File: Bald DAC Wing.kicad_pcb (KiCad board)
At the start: 4 copper layers, 62.2 x 46.5 mm, 46 parts, among them J1 PWR, J10 Ctrl Debug, J11 BNC_B, J13 Feather Debug, J2 DAC_A_Out, J3 DAC_B_Out, J4 BNC_Z, J5 Z_Out, J6 Feather, J7 Data Debug Low, J8 BNC_A, J9 Data Debug High, U1 AD5447, U2 AD8065ARTZ, U3 AD8065ARTZ, U4 74LVC574APWR, U5 74LVC574APWR, U6 74LVC1G04, U7 REF3425

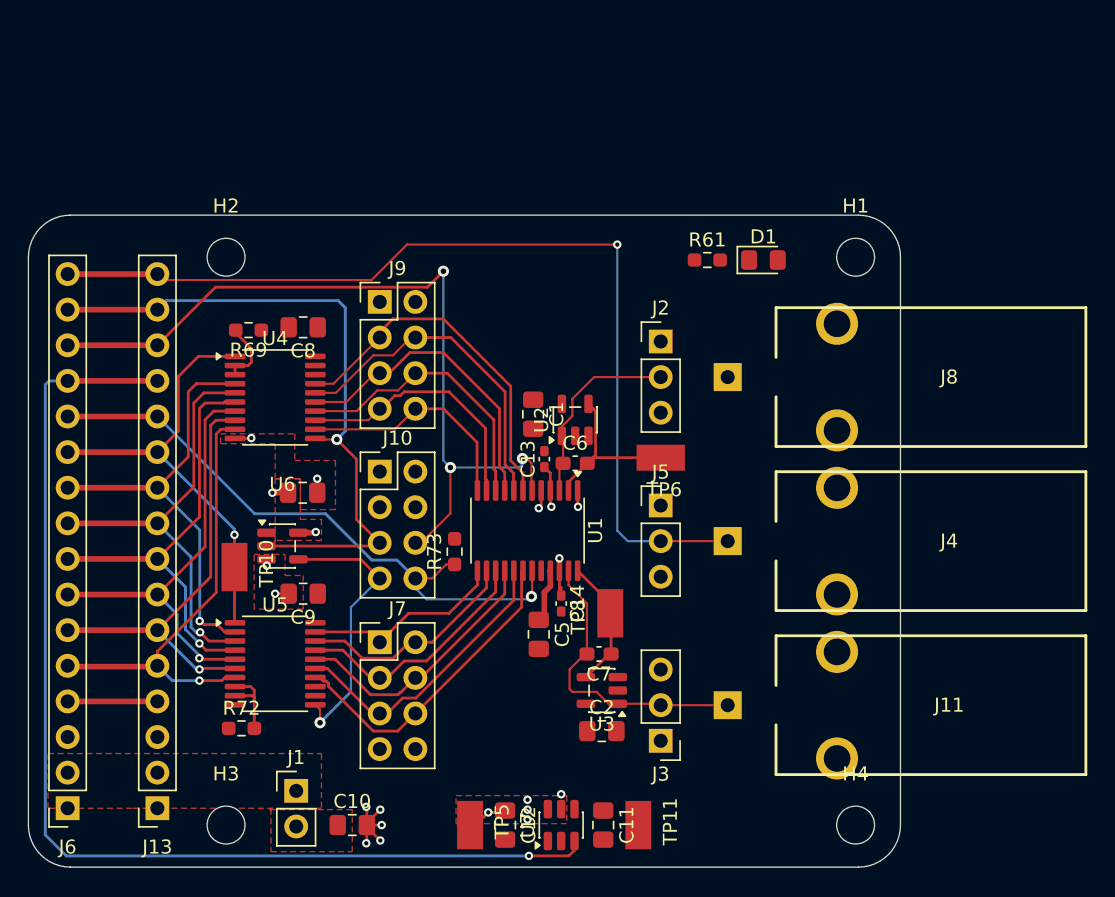
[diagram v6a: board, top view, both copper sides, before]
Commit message: time to clean-up silks.
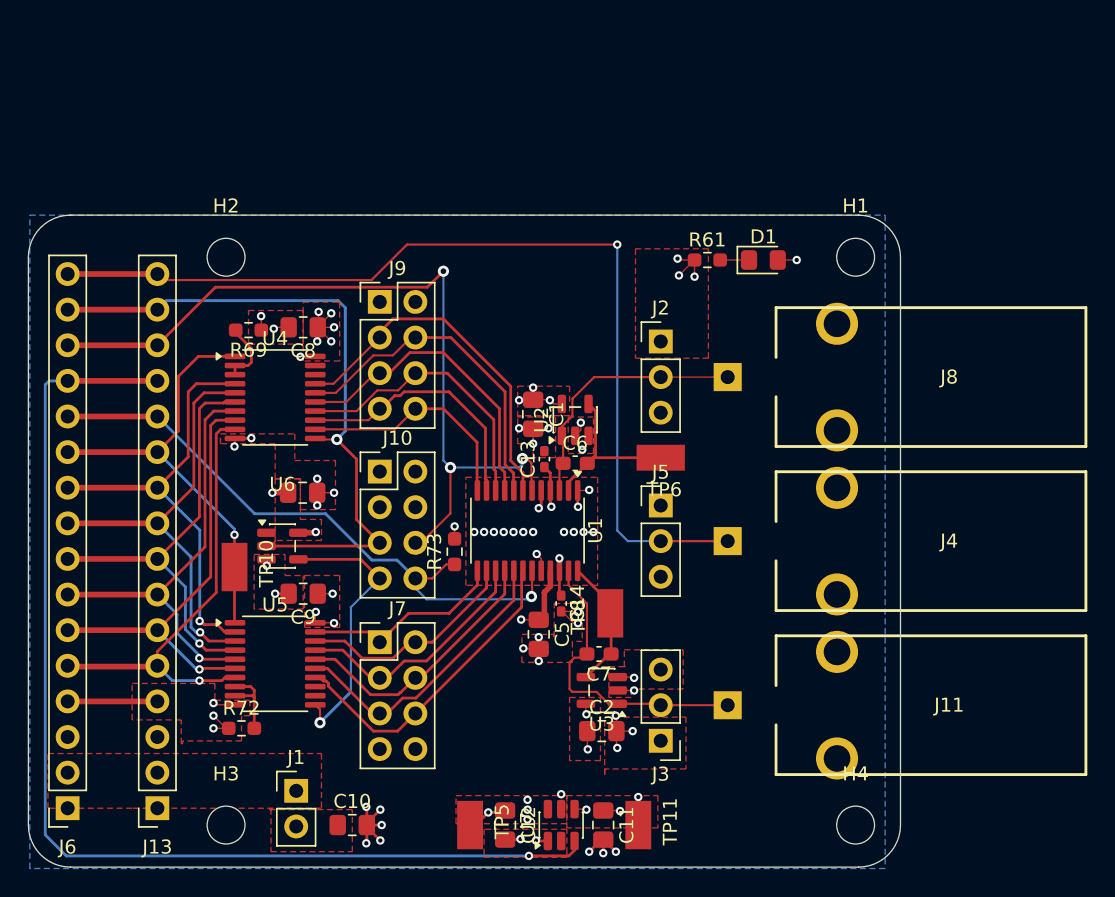
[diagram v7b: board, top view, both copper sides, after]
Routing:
- net GND: track 19.3 -> 55.7 mm, vias 11 -> 55
- net +3V3: track 6.27 -> 30.2 mm, vias 2 -> 22
- net /OUT_A: track 13.9 -> 18.2 mm
- net Net-(D1-K): track 0.00 -> 1.90 mm
- net +2V5: track 9.34 -> 7.91 mm
- net /DB3: track 17.7 -> 16.5 mm
- net /DB1: track 20.9 -> 19.9 mm
- net /DB5: track 14.6 -> 13.5 mm
- net /DB9: track 22.2 -> 21.2 mm
- net /DB10: track 24.1 -> 23.2 mm
- net /Z_Blank: track 69.2 -> 68.6 mm
- net Net-(U1-IOUTA): track 12.6 -> 12.0 mm
- added copper zone on B.Cu, net GND
